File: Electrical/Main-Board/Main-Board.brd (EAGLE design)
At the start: 84 x 100 mm, 41 parts, among them IC1 ATMEGA16A-PU, IC10 TLE4966L, IC2 ATMEGA16A-PU, IC3 AZ1117CH-ADJTRG1, IC4 AZ1117CH-5.0TRG1DITR-ND, IC5 LM2904DRG3, IC6 TLE4966L, IC7 TLE4966L, IC8 TLE4966L, IC9 TLE4966L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

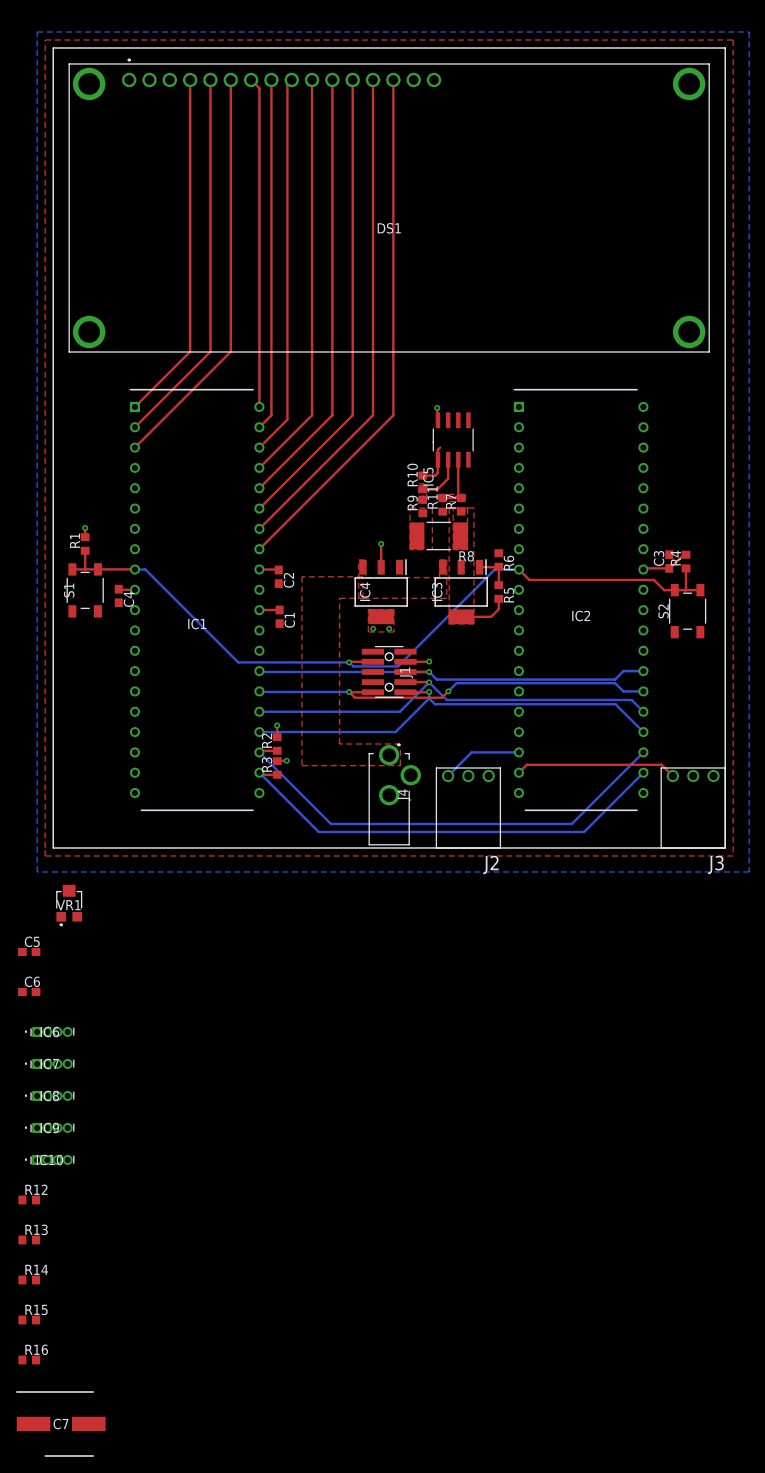
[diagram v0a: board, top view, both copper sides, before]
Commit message: Added the final components to the schmatic and updated the layout
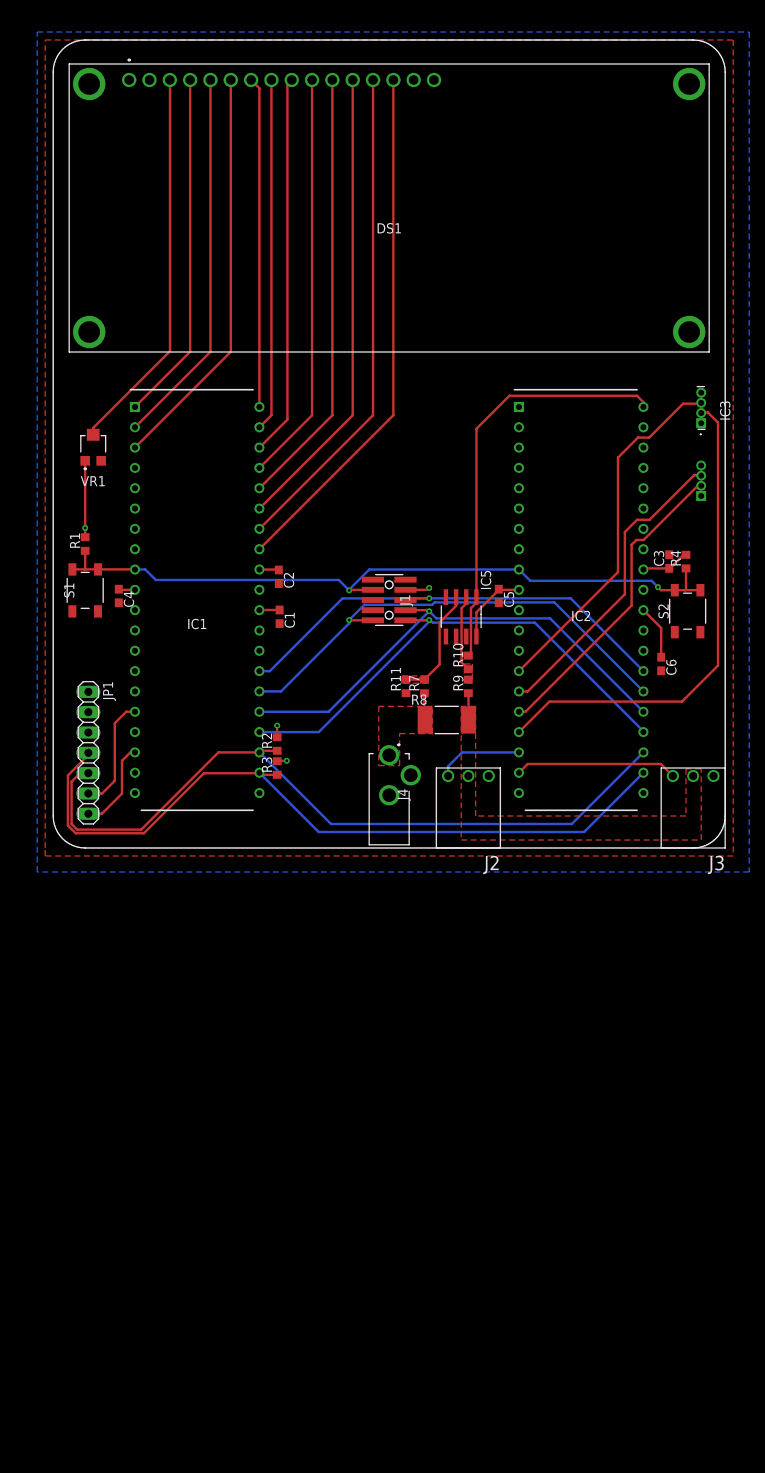
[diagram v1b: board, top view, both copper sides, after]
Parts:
- removed C7: EEEFK1J220P, SamacSys_Parts:CAPAE800X650N
- removed IC10, IC7, IC8, IC9: TLE4966L, SamacSys_Parts:TLE4966L
- removed IC4: AZ1117CH-5.0TRG1DITR-ND, SamacSys_Parts:SOT230P700X180-4N
- removed R12, R13, R14, R15, R16: 1.2K/5%, rcl:R0603
- removed R5: 200R/5%, rcl:R0603
- removed R6: 866R/5%, rcl:R0603
- added JP1: (no value), pinhead:1X07
- IC3: value AZ1117CH-ADJTRG1 -> TLE4966L; device SamacSys_Parts:SOT230P700X170-4N -> SamacSys_Parts:TLE4966L
- moved IC6 106.7 mm to (39.0, 5.00), flipped to the bottom, turned to 90 degrees
- moved C6 89.0 mm to (34.0, -16.0), turned to 270 degrees
- moved C5 73.7 mm to (13.7, -7.50), turned to 270 degrees
- moved VR1 57.1 mm to (-37.0, 11.0)
- moved IC3 36.7 mm to (39.0, 14.1), turned to 90 degrees
- moved R10 23.2 mm to (9.90, -15.8)
- moved R9 23.2 mm to (9.90, -18.8)
- moved R11 23.2 mm to (2.10, -18.8)
- moved R7 23.2 mm to (4.40, -18.8)
- moved R8 23.0 mm to (7.20, -23.0), turned to 0 degrees
- moved IC5 22.1 mm to (9.00, -10.1), turned to 270 degrees
- moved J1 9.00 mm to (0.00, -8.00)
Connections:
- net +7.5V renamed MOTOR_VCC
- removed net +12V: C7.1, IC3.3, IC4.3, J4.1
- removed net DABDA: IC3.2, IC3.4, R5.2, R7.1, R8.1
- removed net LOWER-DISK-LIMIT: IC2.17
- removed net UPPER-DISK-LIMIT: IC2.16
- removed net W3R355: IC3.1, R5.1, R6.2
- new net HALL_DIR-LOWER: IC2.16, IC6.2
- new net HALL_DIR-UPPER: IC2.17, IC3.2
- new net HALL_SPEED-LOWER: IC2.15, IC6.3
- new net HALL_SPEED-UPPER: IC2.14, IC3.3
- new net RGB-INT: IC1.16, JP1.6
- new net RGB-LED: IC1.18, JP1.7
- net +5V/1: now also IC3.1, IC6.1, J4.1, JP1.1, R7.1, R8.1; no longer IC4.2, IC4.4
- net GND: now also IC3.4, IC6.4, JP1.2; no longer C7.2, IC4.1, R6.1
- net SCL: now also JP1.4
- net SDA: now also JP1.5
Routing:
- net HALL_DIR-UPPER: track 0.00 -> 61.3 mm
- net N$2: track 0.00 -> 48.3 mm
- net MOTOR_OVER-CURRENT: track 5.33 -> 52.3 mm
- net HALL_SPEED-UPPER: track 0.00 -> 45.1 mm
- net HALL_DIR-LOWER: track 0.00 -> 38.9 mm
- net HALL_SPEED-LOWER: track 0.00 -> 38.6 mm
- net SCL: track 56.5 -> 94.1 mm
- net SDA: track 57.8 -> 93.3 mm
- net +5V/1: track 24.4 -> 48.2 mm, vias 8 -> 4
- net RGB-INT: track 0.00 -> 14.3 mm
- net RGB-LED: track 0.00 -> 11.4 mm
- net TDO: track 52.5 -> 60.4 mm, vias 2 -> 1
- net RST: track 97.7 -> 89.9 mm, vias 1 -> 2
- net TCK: track 55.3 -> 62.8 mm
- net N$1: track 6.52 -> 14.0 mm
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- removed copper zone on layer 1, net +12V
- removed copper zone on layer 1, net DABDA
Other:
- board size 84 x 100 mm -> 84 x 101 mm

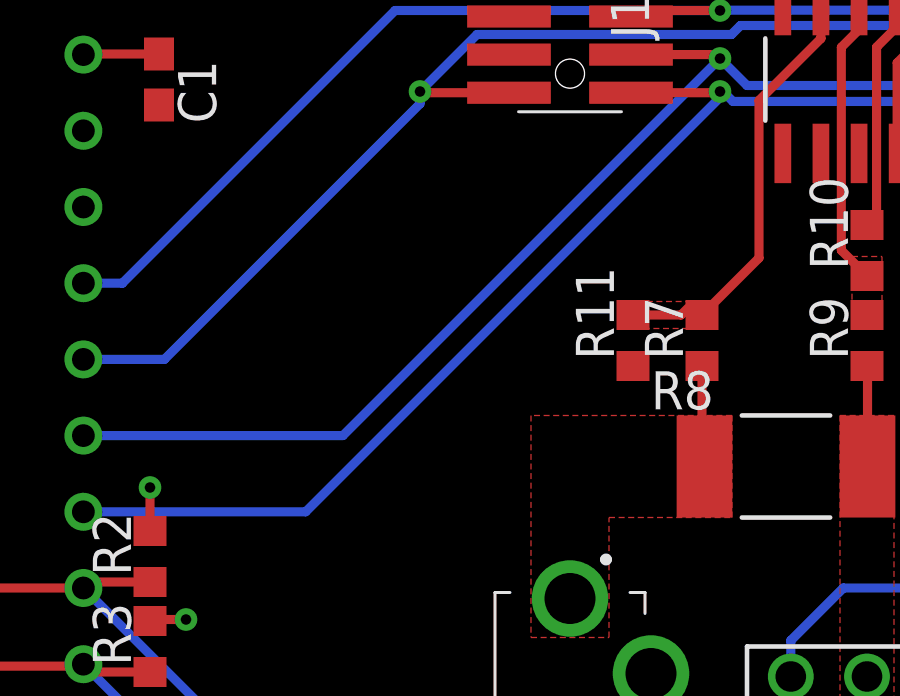
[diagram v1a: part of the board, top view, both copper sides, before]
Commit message: LCD is wrong, need to finish teh new footprint for it.
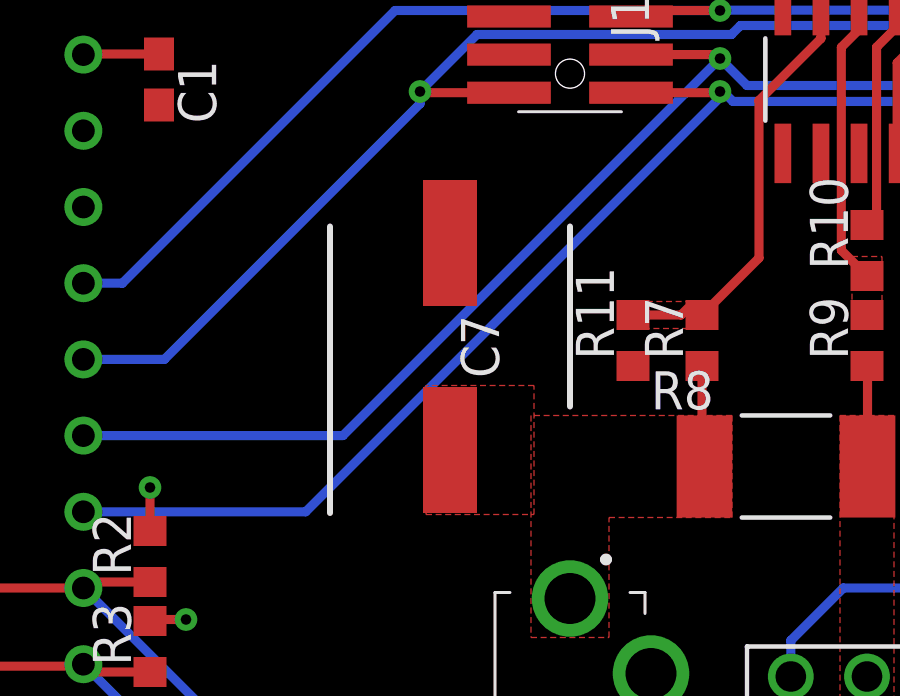
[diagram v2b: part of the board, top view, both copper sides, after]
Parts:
- added C7: EEEFK1J220P, SamacSys_Parts:CAPAE800X650N
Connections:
- net +5V/1: now also C7.1
- net GND: now also C7.2
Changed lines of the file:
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@@
 <wire x1="-38" y1="-39" x2="38" y2="-39" width="0" layer="20"/>
 <wire x1="38" y1="-39" x2="42" y2="-35" width="0" layer="20" curve="90"/>
+<dimension x1="-37.5" y1="56.5" x2="37.6" y2="56.5" x3="0.05" y3="64.5" textsize="1.778" layer="49"/>
 </plain>
 <attributes>
@@
 <attribute name="VALUE" x="39" y="15.663" size="1.27" layer="27" rot="R90" align="center"/>
 </element>
+<element name="C7" library="SamacSys_Parts" package="CAPAE800X650N" value="EEEFK1J220P" x="-4" y="-19" smashed="yes" rot="R90">
+<attribute name="DESCRIPTION" value="Panasonic Aluminium Electrolytic Capacitor 22uF 63V dc 8mm E FK SMD Series, Surface Mount Electrolytic, +/-20%" x="-4" y="-19" size="1.778" layer="27" rot="R90" display="off"/>
+<attribute name="HEIGHT" value="6.5mm" x="-4" y="-19" size="1.778" layer="27" rot="R90" display="off"/>
+<attribute name="MANUFACTURER_NAME" value="Panasonic" x="-4" y="-19" size="1.778" layer="27" rot="R90" display="off"/>
+<attribute name="MANUFACTURER_PART_NUMBER" value="EEEFK1J220P" x="-4" y="-19" size="1.778" layer="27" rot="R90" display="off"/>
+<attribute name="MOUSER_PART_NUMBER" value="" x="-4" y="-19" size="1.778" layer="27" rot="R90" display="off"/>
+<attribute name="MOUSER_PRICE-STOCK" value="" x="-4" y="-19" size="1.778" layer="27" rot="R90" display="off"/>
+<attribute name="NAME" x="-3" y="-19" size="1.27" layer="25" rot="R90" align="center"/>
+<attribute name="RS_PART_NUMBER" value="7083598P" x="-4" y="-19" size="1.778" layer="27" rot="R90" display="off"/>
+<attribute name="RS_PRICE-STOCK" value="http://uk.rs-online.com/web/p/products/7083598P" x="-4" y="-19" size="1.778" layer="27" rot="R90" display="off"/>
+<attribute name="VALUE" x="-4" y="-19" size="1.27" layer="27" rot="R90" align="center"/>
+</element>
 </elements>
 <signals>
@@
 <contactref element="IC6" pad="4"/>
 <contactref element="IC3" pad="4"/>
+<contactref element="C7" pad="2"/>
 </signal>
 <signal name="+5V/1">
@@
 <contactref element="IC6" pad="1"/>
 <contactref element="IC3" pad="1"/>
+<contactref element="C7" pad="1"/>
+<polygon width="0.15" layer="1" thermals="no">
+<vertex x="-1.2" y="-20.3"/>
+<vertex x="-4.8" y="-20.3"/>
+<vertex x="-4.8" y="-24.6"/>
+<vertex x="-1.2" y="-24.6"/>
+</polygon>
 </signal>
 <signal name="TCK">

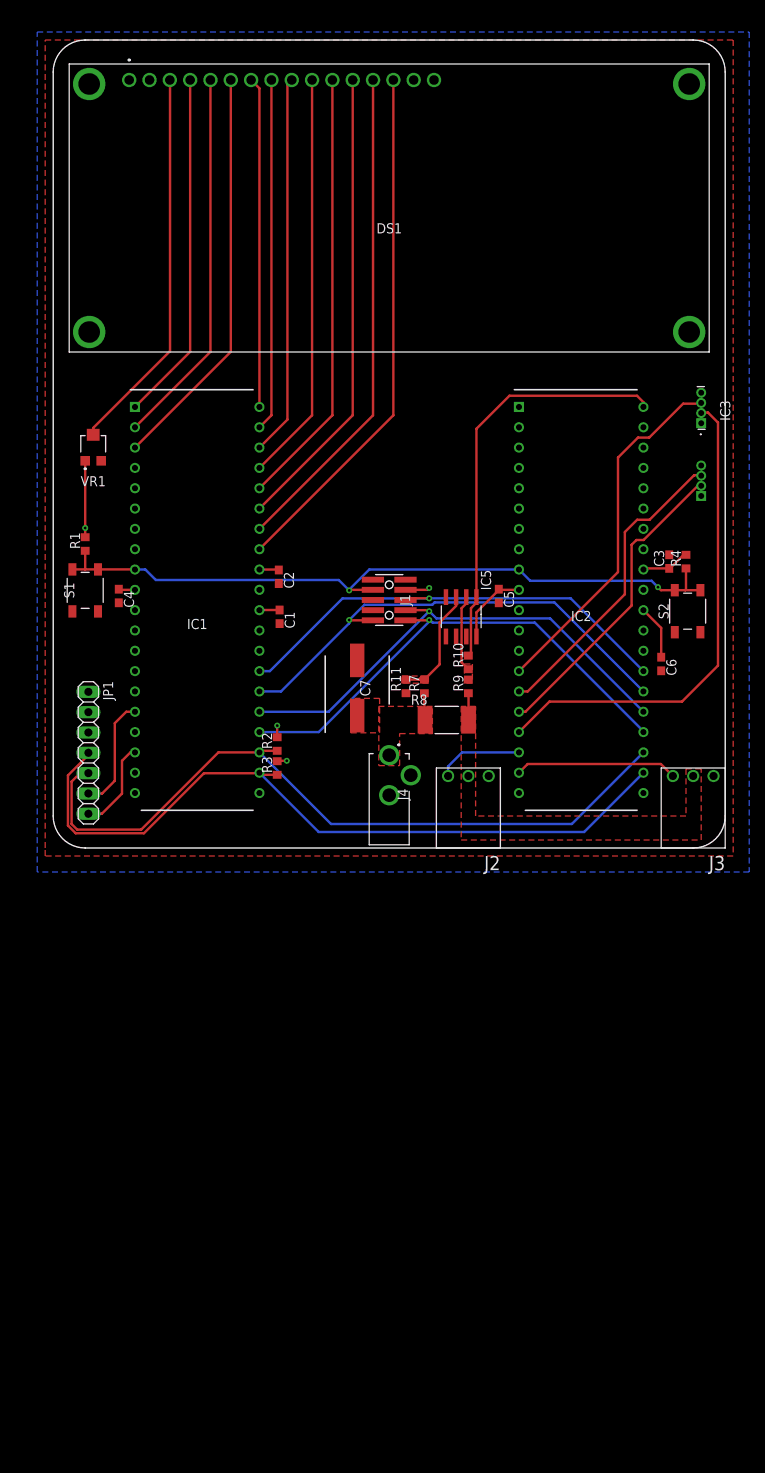
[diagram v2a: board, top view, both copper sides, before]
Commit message: Updated display footprint and fixed layout to suit it.
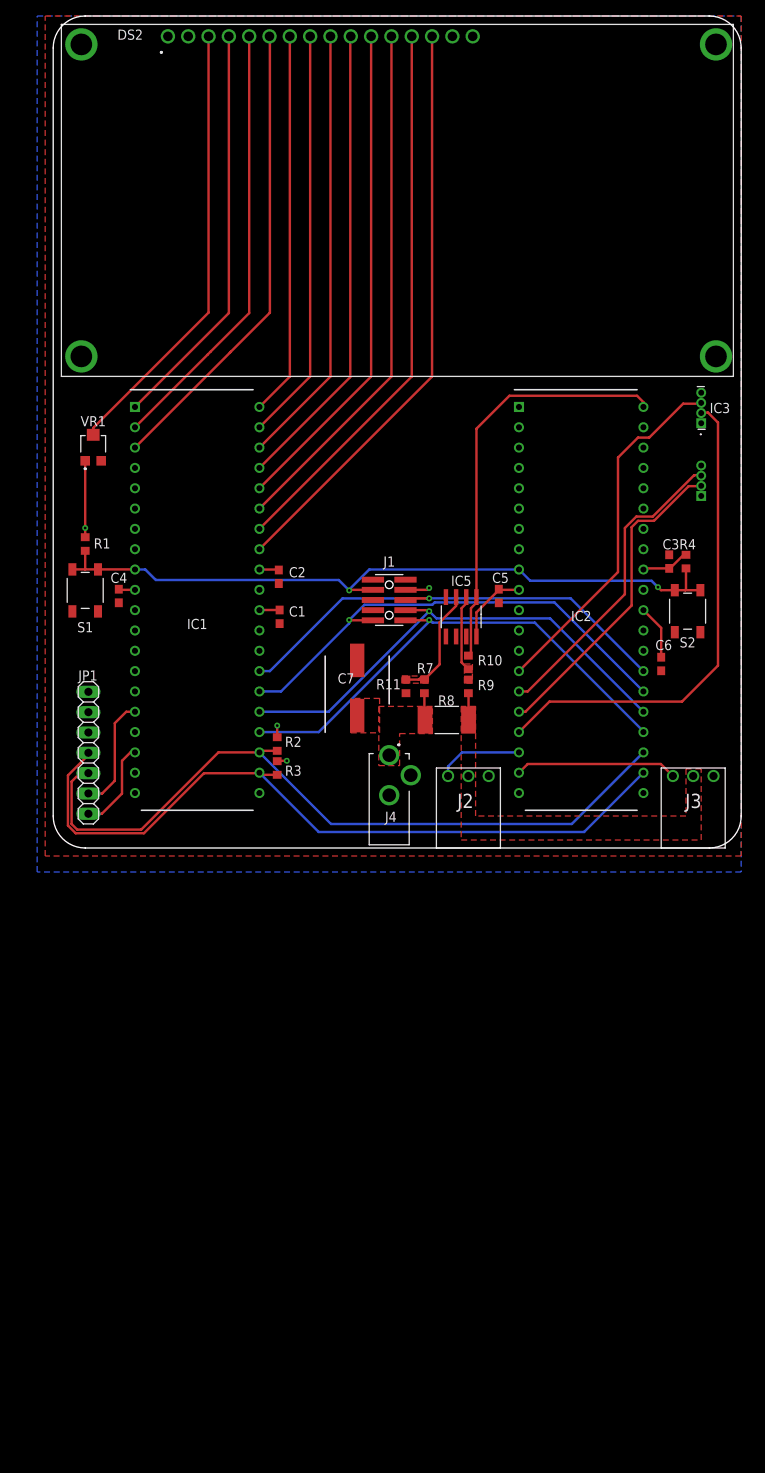
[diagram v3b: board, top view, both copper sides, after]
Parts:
- removed DS1: NHD-0216XZ-FSW-GBW, SamacSys_Parts:NHD0216XZFSWGBW
- added DS2: JM16A, JM16A-Vanheden:JM16A
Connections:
- net +5V/1: now also DS2.2; no longer DS1.2
- net GND: now also DS2.1, DS2.MOUNT-1, DS2.MOUNT-2, DS2.MOUNT-3, DS2.MOUNT-4; no longer DS1.1
- net LCD-DB0: now also DS2.7; no longer DS1.7
- net LCD-DB1: now also DS2.8; no longer DS1.8
- net LCD-DB2: now also DS2.9; no longer DS1.9
- net LCD-DB3: now also DS2.10; no longer DS1.10
- net LCD-DB4: now also DS2.11; no longer DS1.11
- net LCD-DB5: now also DS2.12; no longer DS1.12
- net LCD-DB6: now also DS2.13; no longer DS1.13
- net LCD-DB7: now also DS2.14; no longer DS1.14
- net LCD-E: now also DS2.6; no longer DS1.6
- net LCD-R/W: now also DS2.5; no longer DS1.5
- net LCD-RS: now also DS2.4; no longer DS1.4
- net N$2: now also DS2.3; no longer DS1.3
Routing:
- net LCD-E: track 50.9 -> 58.4 mm
- net LCD-DB6: track 62.0 -> 69.5 mm
- net LCD-DB4: track 54.8 -> 62.3 mm
- net LCD-R/W: track 47.3 -> 54.8 mm
- net LCD-DB7: track 65.6 -> 73.0 mm
- net LCD-DB5: track 58.4 -> 65.9 mm
- net LCD-DB2: track 47.6 -> 55.1 mm
- net LCD-DB1: track 44.0 -> 51.5 mm
- net LCD-DB3: track 51.2 -> 58.7 mm
- net LCD-RS: track 43.7 -> 51.2 mm
- net N$2: track 48.3 -> 55.8 mm
- net LCD-DB0: track 41.3 -> 47.9 mm
- net HALL_DIR-LOWER: track 38.9 -> 40.2 mm
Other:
- board size 84 x 101 mm -> 86 x 104 mm

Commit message: Final PCB. Added GERBER files for MF
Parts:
- added JP2: (no value), pinhead:1X02
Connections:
- new net N$3: IC2.2, JP2.2
- net GND: now also JP2.1
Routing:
- net N$3: track 0.00 -> 8.23 mm
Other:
- board text added: "TSIU51: MikroDator projekt Skittle Sort 06/02-2020 Version: 1 JS"
